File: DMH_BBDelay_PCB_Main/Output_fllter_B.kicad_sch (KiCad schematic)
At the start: 15 parts, among them U21 TL072

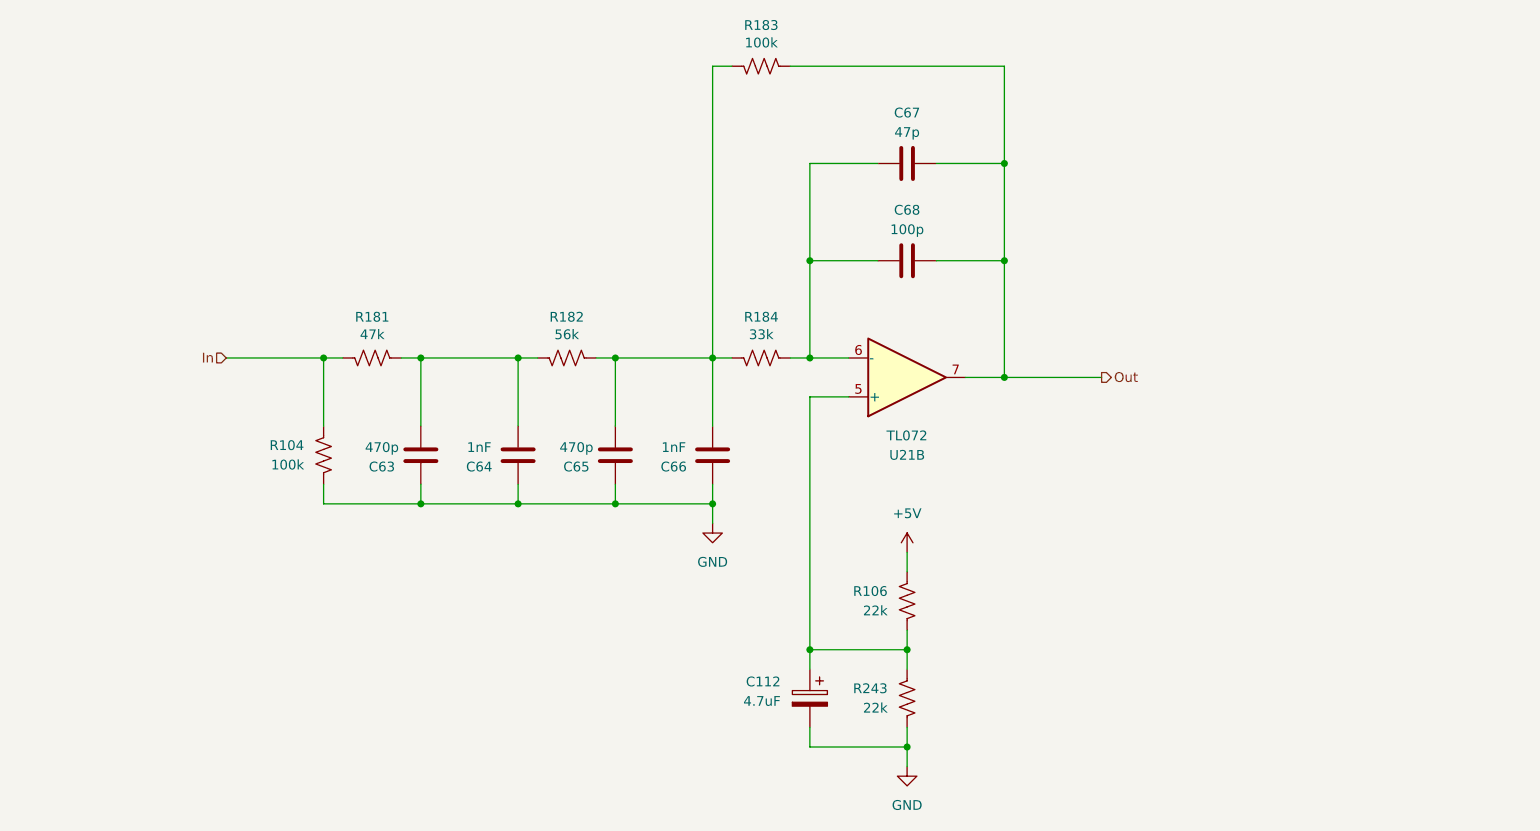
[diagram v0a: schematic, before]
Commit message: Inserted compander into channel B path
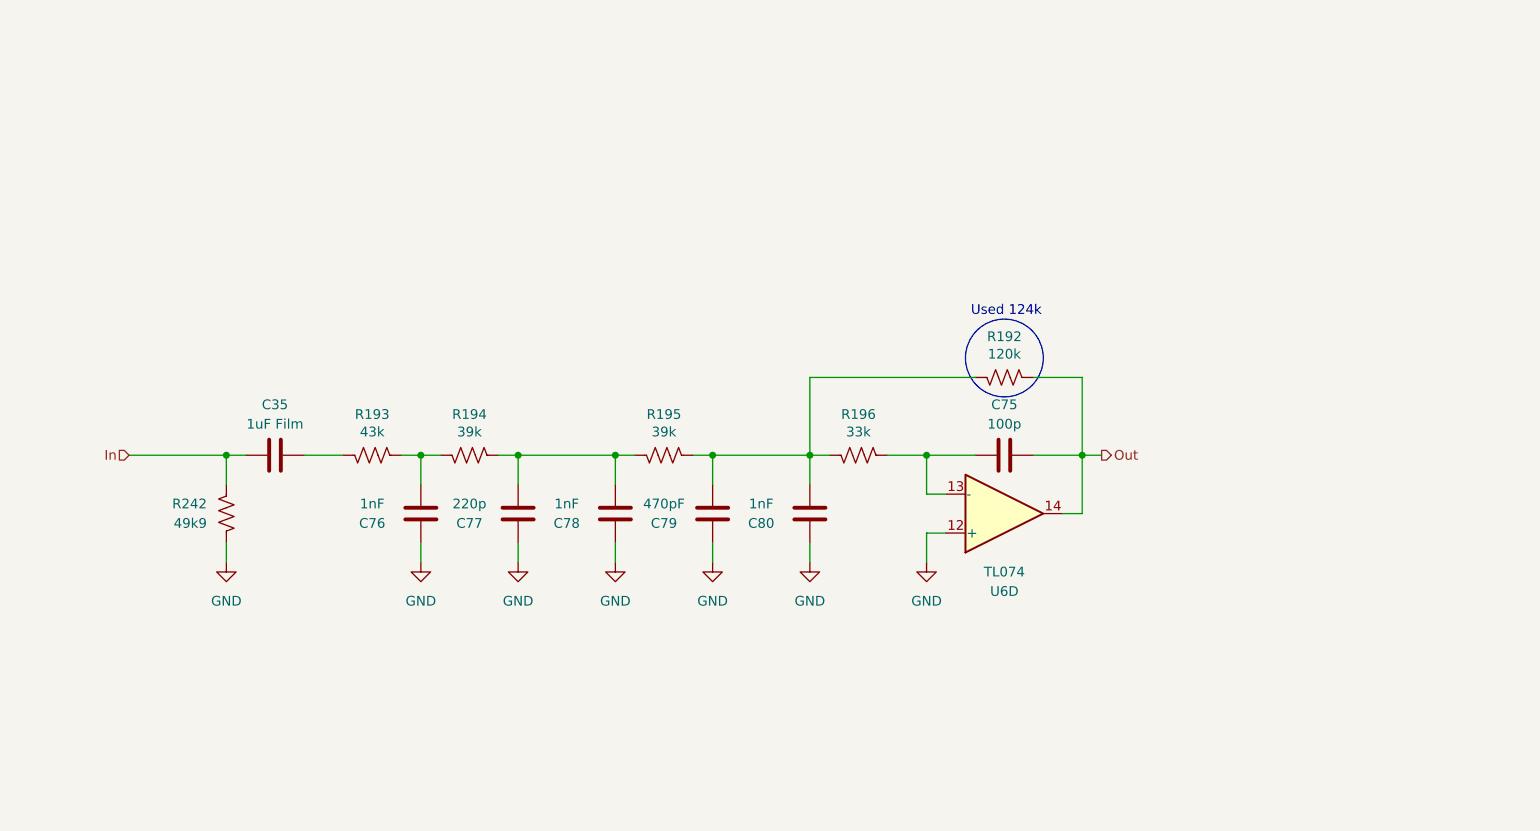
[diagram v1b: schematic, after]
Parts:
- removed C112: 4.7uF, Capacitor_THT:CP_Radial_D4.0mm_P1.50mm, symbol Device:C_Polarized
- removed C63, C65: 470p, Capacitor_THT:C_Disc_D3.0mm_W2.0mm_P2.50mm, symbol Device:C
- removed C64, C66: 1nF, Capacitor_THT:C_Disc_D3.0mm_W2.0mm_P2.50mm, symbol Device:C
- removed C67: 47p, Capacitor_THT:C_Disc_D3.0mm_W2.0mm_P2.50mm, symbol Device:C
- removed C68: 100p, Capacitor_THT:C_Disc_D3.0mm_W2.0mm_P2.50mm, symbol Device:C
- removed R104, R183: 100k, Resistor_THT:R_Axial_DIN0207_L6.3mm_D2.5mm_P7.62mm_Horizontal, symbol Device:R_US
- removed R106, R243: 22k, Resistor_THT:R_Axial_DIN0207_L6.3mm_D2.5mm_P7.62mm_Horizontal, symbol Device:R_US
- removed R181: 47k, Resistor_THT:R_Axial_DIN0207_L6.3mm_D2.5mm_P7.62mm_Horizontal, symbol Device:R_US
- removed R182: 56k, Resistor_THT:R_Axial_DIN0207_L6.3mm_D2.5mm_P7.62mm_Horizontal, symbol Device:R_US
- removed R184: 33k, Resistor_THT:R_Axial_DIN0207_L6.3mm_D2.5mm_P7.62mm_Horizontal, symbol Device:R_US
- removed U21: TL072, Package_DIP:DIP-8_W7.62mm_Socket, symbol Amplifier_Operational:TL072
- added C35: 1uF Film, Capacitor_THT:C_Disc_D7.5mm_W5.0mm_P5.00mm, symbol Device:C
- added C75: 100p, Capacitor_THT:C_Disc_D3.0mm_W2.0mm_P2.50mm, symbol Device:C
- added C76, C78, C80: 1nF, Capacitor_THT:C_Disc_D4.3mm_W1.9mm_P5.00mm, symbol Device:C
- added C77: 220p, Capacitor_THT:C_Disc_D4.3mm_W1.9mm_P5.00mm, symbol Device:C
- added C79: 470pF, Capacitor_THT:C_Disc_D4.3mm_W1.9mm_P5.00mm, symbol Device:C
- added R192: 120k, Resistor_THT:R_Axial_DIN0207_L6.3mm_D2.5mm_P7.62mm_Horizontal, symbol Device:R_US
- added R193: 43k, Resistor_THT:R_Axial_DIN0207_L6.3mm_D2.5mm_P7.62mm_Horizontal, symbol Device:R_US
- added R194, R195: 39k, Resistor_THT:R_Axial_DIN0207_L6.3mm_D2.5mm_P7.62mm_Horizontal, symbol Device:R_US
- added R196: 33k, Resistor_THT:R_Axial_DIN0207_L6.3mm_D2.5mm_P7.62mm_Horizontal, symbol Device:R_US
- added R242: 49k9, Resistor_THT:R_Axial_DIN0207_L6.3mm_D2.5mm_P7.62mm_Horizontal, symbol Device:R_US
- added U6: TL074, Package_DIP:DIP-14_W7.62mm_Socket, symbol Amplifier_Operational:TL074
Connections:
- net GND: now also C76.1, C77.1, C78.1, C79.1, C80.1, R242.1, U6.12 (+)
- net In: now also C35.1, R242.2
- net Out: now also C75.2, R192.2, U6.14
- new net: C79.2, C80.2, R192.1, R195.2, R196.1
- new net: C75.1, R196.2, U6.13 (-)
- new net: C77.2, C78.2, R194.2, R195.1
- new net: C76.2, R193.2, R194.1
- new net: C35.2, R193.1
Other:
- note added: "Used 124k"
- title: (none) -> 3205 Delay

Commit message: Adjustments during breadboarding
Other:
- note added: "Used 47k"
- note removed: "Used 124k"
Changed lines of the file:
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@@
 	)
 	(circle
-		(center 139.7 63.5)
+		(center 34.798 83.82)
 		(radius 5.08)
 		(stroke
@@
 		)
 	)
-	(text "Used 124k"
+	(text "Used 47k"
 		(exclude_from_sim no)
-		(at 139.954 57.404 0)
+		(at 24.13 83.82 0)
 		(effects
 			(font

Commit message: More adjustments during breadboarding
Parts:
- removed C35: 1uF Film, Capacitor_THT:C_Disc_D7.5mm_W5.0mm_P5.00mm, symbol Device:C
- added C115: 4.7uF, Capacitor_THT:C_Disc_D4.3mm_W1.9mm_P5.00mm, symbol Device:C
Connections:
- net In: now also C115.1
- net at R193.1: now also C115.2
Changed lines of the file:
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@@
 		(in_pos_files yes)
 		(dnp no)
-		(property "Reference" "C35"
-			(at 44.45 69.596 90)
+		(fields_autoplaced yes)
+		(property "Reference" "C115"
+			(at 44.45 68.58 90)
 			(show_name no)
 			(do_not_autoplace no)
@@
 			)
 		)
-		(property "Value" "1uF Film"
-			(at 44.45 72.136 90)
+		(property "Value" "4.7uF"
+			(at 44.45 71.12 90)
 			(show_name no)
 			(do_not_autoplace no)
@@
 			)
 		)
-		(property "Footprint" "Capacitor_THT:C_Disc_D7.5mm_W5.0mm_P5.00mm"
+		(property "Footprint" "Capacitor_THT:C_Disc_D4.3mm_W1.9mm_P5.00mm"
 			(at 48.26 75.2348 0)
 			(hide yes)
@@
 			)
 		)
-		(property "Function" ""
-			(at 44.45 76.2 0)
-			(show_name no)
-			(do_not_autoplace no)
-			(effects
-				(font
-					(size 1.27 1.27)
-				)
-			)
-		)
 		(pin "1"
 		)
@@
 			(project "DMH_BBDelay_PCB_Main"
 				(path "/58f4306d-5387-4983-bb08-41a2313fd315/53120047-129a-4e0f-876f-6cafa2f18733/b220cd30-3d79-47df-ac4c-a5efb41766f0"
-					(reference "C35")
+					(reference "C115")
 					(unit 1)
 				)

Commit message: Added notes from troubleshooting
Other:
- note added: "This 49.9k resistor seems to have no effect, since this input comes from a OpAmp output directly."
- note added: "This filter seems to be rolling off the signal at 1kHz (C5) already. It should have a -3dB attenuation as of 5kHz only. Try simulating it to see how it can be improved."
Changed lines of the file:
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@@
+		)
+	)
+	(text "This 49.9k resistor seems to have no effect,\nsince this input comes from a OpAmp output directly."
+		(exclude_from_sim no)
+		(at 42.672 102.108 0)
+		(effects
+			(font
+				(size 1.27 1.27)
+			)
 		)
 	)
@@
 		(effects
 			(font
+				(size 1.27 1.27)
+			)
+		)
+	)
+	(text "This filter seems to be rolling off the signal at 1kHz (C5) already.\nIt should have a -3dB attenuation as of 5kHz only.\nTry simulating it to see how it can be improved."
+		(exclude_from_sim no)
+		(at 166.878 51.308 0)
+		(effects
+			(font

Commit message: Removed compander and adjusted feedback
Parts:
- removed R242: 49k9, Resistor_THT:R_Axial_DIN0207_L6.3mm_D2.5mm_P7.62mm_Horizontal, symbol Device:R_US
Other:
- note removed: "This 49.9k resistor seems to have no effect, since this input comes from a OpAmp output directly."
- note removed: "This filter seems to be rolling off the signal at 1kHz (C5) already. It should have a -3dB attenuation as of 5kHz only. Try simulating it to see how it can be improved."
- note removed: "Used 47k"
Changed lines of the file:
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@@
 		(comment 1 "PCB for 10cm Kosmo format synthesizer module")
-	)
-	(circle
-		(center 34.798 83.82)
-		(radius 5.08)
-		(stroke
-			(width 0)
-			(type default)
-		)
-		(fill
-			(type none)
-		)
-	)
-	(text "This 49.9k resistor seems to have no effect,\nsince this input comes from a OpAmp output directly."
-		(exclude_from_sim no)
-		(at 42.672 102.108 0)
-		(effects
-			(font
-				(size 1.27 1.27)
-			)
-		)
-	)
-	(text "Used 47k"
-		(exclude_from_sim no)
-		(at 24.13 83.82 0)
-		(effects
-			(font
-				(size 1.27 1.27)
-			)
-		)
-	)
-	(text "This filter seems to be rolling off the signal at 1kHz (C5) already.\nIt should have a -3dB attenuation as of 5kHz only.\nTry simulating it to see how it can be improved."
-		(exclude_from_sim no)
-		(at 166.878 51.308 0)
-		(effects
-			(font
-				(size 1.27 1.27)
-			)
-		)
 	)
 	(junction
@@
 	)
 	(junction
-		(at 38.1 76.2)
-		(diameter 0)
-		(color 0 0 0 0)
-	)
-	(junction
 		(at 101.6 76.2)
 		(diameter 0)
@@
 	(wire
 		(pts
-			(xy 38.1 87.63) (xy 38.1 90.17)
-		)
-		(stroke
-			(width 0)
-			(type default)
-		)
-	)
-	(wire
-		(pts
 			(xy 99.06 76.2) (xy 101.6 76.2)
 		)
@@
 	(wire
 		(pts
-			(xy 38.1 76.2) (xy 38.1 80.01)
-		)
-		(stroke
-			(width 0)
-			(type default)
-		)
-	)
-	(wire
-		(pts
-			(xy 38.1 76.2) (xy 40.64 76.2)
+			(xy 25.4 76.2) (xy 40.64 76.2)
 		)
 		(stroke
@@
 		(pts
 			(xy 114.3 66.04) (xy 114.3 76.2)
-		)
-		(stroke
-			(width 0)
-			(type default)
-		)
-	)
-	(wire
-		(pts
-			(xy 25.4 76.2) (xy 38.1 76.2)
 		)
 		(stroke
@@
 	)
 	(symbol
-		(lib_id "power:GND")
-		(at 38.1 90.17 0)
-		(unit 1)
-		(body_style 1)
-		(exclude_from_sim no)
-		(in_bom yes)
-		(on_board yes)
-		(in_pos_files yes)
-		(dnp no)
-		(fields_autoplaced yes)
-		(property "Reference" "#PWR0290"
-			(at 38.1 96.52 0)
-			(hide yes)
-			(show_name no)
-			(do_not_autoplace no)
-			(effects
-				(font
-					(size 1.27 1.27)
-				)
-			)
-		)
-		(property "Value" "GND"
-			(at 38.1 95.25 0)
-			(show_name no)
-			(do_not_autoplace no)
-			(effects
-				(font
-					(size 1.27 1.27)
-				)
-			)
-		)
-		(property "Footprint" ""
-			(at 38.1 90.17 0)
-			(hide yes)
-			(show_name no)
-			(do_not_autoplace no)
-			(effects
-				(font
-					(size 1.27 1.27)
-				)
-			)
-		)
-		(property "Datasheet" ""
-			(at 38.1 90.17 0)
-			(hide yes)
-			(show_name no)
-			(do_not_autoplace no)
-			(effects
-				(font
-					(size 1.27 1.27)
-				)
-			)
-		)
-		(property "Description" "Power symbol creates a global label with name \"GND\" , ground"
-			(at 38.1 90.17 0)
-			(hide yes)
-			(show_name no)
-			(do_not_autoplace no)
-			(effects
-				(font
-					(size 1.27 1.27)
-				)
-			)
-		)
-		(pin "1"
-		)
-		(instances
-			(project "DMH_BBDelay_PCB_Main"
-				(path "/58f4306d-5387-4983-bb08-41a2313fd315/53120047-129a-4e0f-876f-6cafa2f18733/b220cd30-3d79-47df-ac4c-a5efb41766f0"
-					(reference "#PWR0290")
-					(unit 1)
-				)
-			)
-		)
-	)
-	(symbol
 		(lib_id "Device:C")
 		(at 44.45 76.2 90)
@@
 					(unit 1)
 				)
-			)
-		)
-	)
-	(symbol
-		(lib_id "Device:R_US")
-		(at 38.1 83.82 0)
-		(mirror x)
-		(unit 1)
-		(body_style 1)
-		(exclude_from_sim no)
-		(in_bom yes)
-		(on_board yes)
-		(in_pos_files yes)
-		(dnp no)
-		(property "Reference" "R242"
-			(at 35.56 82.5499 0)
-			(show_name no)
-			(do_not_autoplace no)
-			(effects
-				(font
-					(size 1.27 1.27)
-				)
-				(justify right)
-			)
-		)
-		(property "Value" "49k9"
-			(at 35.56 85.0899 0)
-			(show_name no)
-			(do_not_autoplace no)
-			(effects
-				(font
-					(size 1.27 1.27)
-				)
-				(justify right)
-			)
-		)
-		(property "Footprint" "Resistor_THT:R_Axial_DIN0207_L6.3mm_D2.5mm_P7.62mm_Horizontal"
-			(at 39.116 83.566 90)
-			(hide yes)
-			(show_name no)
-			(do_not_autoplace no)
-			(effects
-				(font
-					(size 1.27 1.27)
-				)
-			)
-		)
-		(property "Datasheet" ""
-			(at 38.1 83.82 0)
-			(hide yes)
-			(show_name no)
-			(do_not_autoplace no)
-			(effects
-				(font
-					(size 1.27 1.27)
-				)
-			)
-		)
-		(property "Description" "Resistor, US symbol"
-			(at 38.1 83.82 0)
-			(hide yes)
-			(show_name no)
-			(do_not_autoplace no)
-			(effects
-				(font
-					(size 1.27 1.27)
-				)
-			)
-		)
-		(pin "2"
-		)
-		(pin "1"
-		)
-		(instances
-			(project "DMH_BBDelay_PCB_Main"
-				(path "/58f4306d-5387-4983-bb08-41a2313fd315/53120047-129a-4e0f-876f-6cafa2f18733/b220cd30-3d79-47df-ac4c-a5efb41766f0"
-					(reference "R242")
-					(unit 1)
-				)

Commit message: Synced channel A and B schematics
... and applied several minor improvements and optimizations.
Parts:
- removed C115: 4.7uF, Capacitor_THT:C_Disc_D4.3mm_W1.9mm_P5.00mm, symbol Device:C
- removed C77: 220p, Capacitor_THT:C_Disc_D4.3mm_W1.9mm_P5.00mm, symbol Device:C
- removed C79: 470pF, Capacitor_THT:C_Disc_D4.3mm_W1.9mm_P5.00mm, symbol Device:C
- added C58: 1uF Film, Capacitor_THT:C_Disc_D7.5mm_W5.0mm_P5.00mm, symbol Device:C
- C80: value 1nF -> 1.5nF
- R194: value 39k -> 43k
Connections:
- net In: now also C58.1
- net at R193.1: now also C58.2
